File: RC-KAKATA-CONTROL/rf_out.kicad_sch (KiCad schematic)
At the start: 4 parts

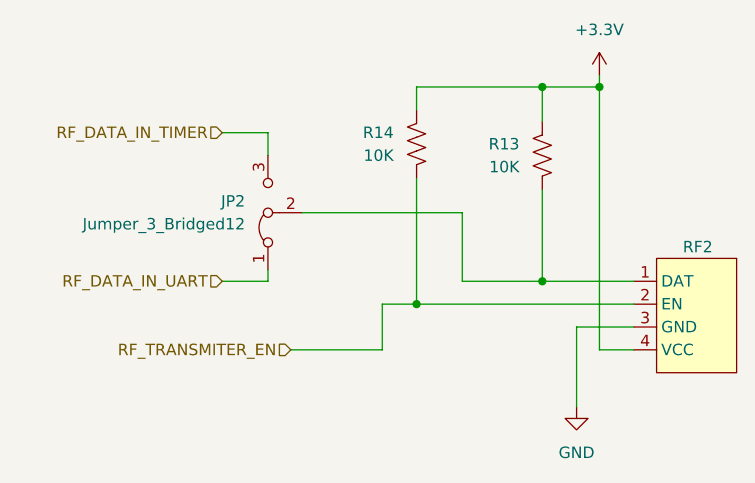
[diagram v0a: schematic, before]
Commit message: Colocadas todas las piezas Verificacion de conexiones de los puertos UART - I2C - SPI Realizadas todas las conexiones Verificados los errores
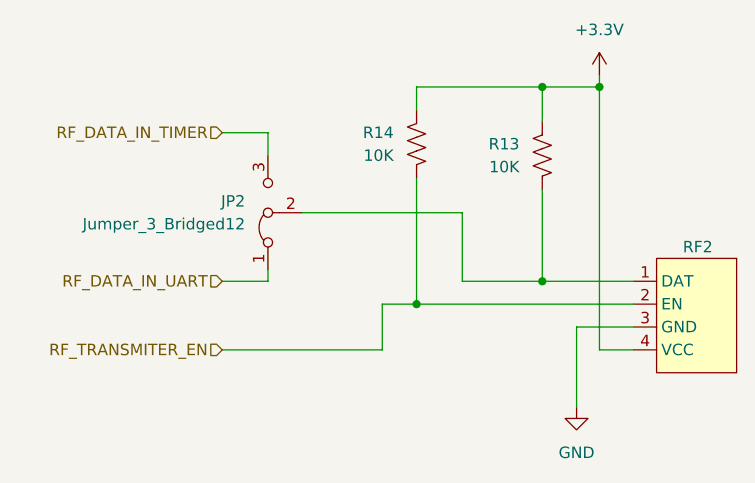
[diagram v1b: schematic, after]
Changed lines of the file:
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@@
 	(generator "eeschema")
 	(generator_version "9.0")
-	(paper "A4")
+	(paper "USLedger")
 	(title_block
 		(title "RC-KAKATA-CONTROL")
@@
 	(wire
 		(pts
-			(xy 58.42 85.09) (xy 68.58 85.09)
+			(xy 50.8 85.09) (xy 68.58 85.09)
 		)
 		(stroke
@@
 	(hierarchical_label "RF_TRANSMITER_EN"
 		(shape input)
-		(at 58.42 85.09 180)
+		(at 50.8 85.09 180)
 		(effects
 			(font
